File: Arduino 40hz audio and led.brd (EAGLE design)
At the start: 122.7 x 100 mm, 29 parts, among them IC1 LM7805, IC2 IRL-Z44N, IC3 LM741

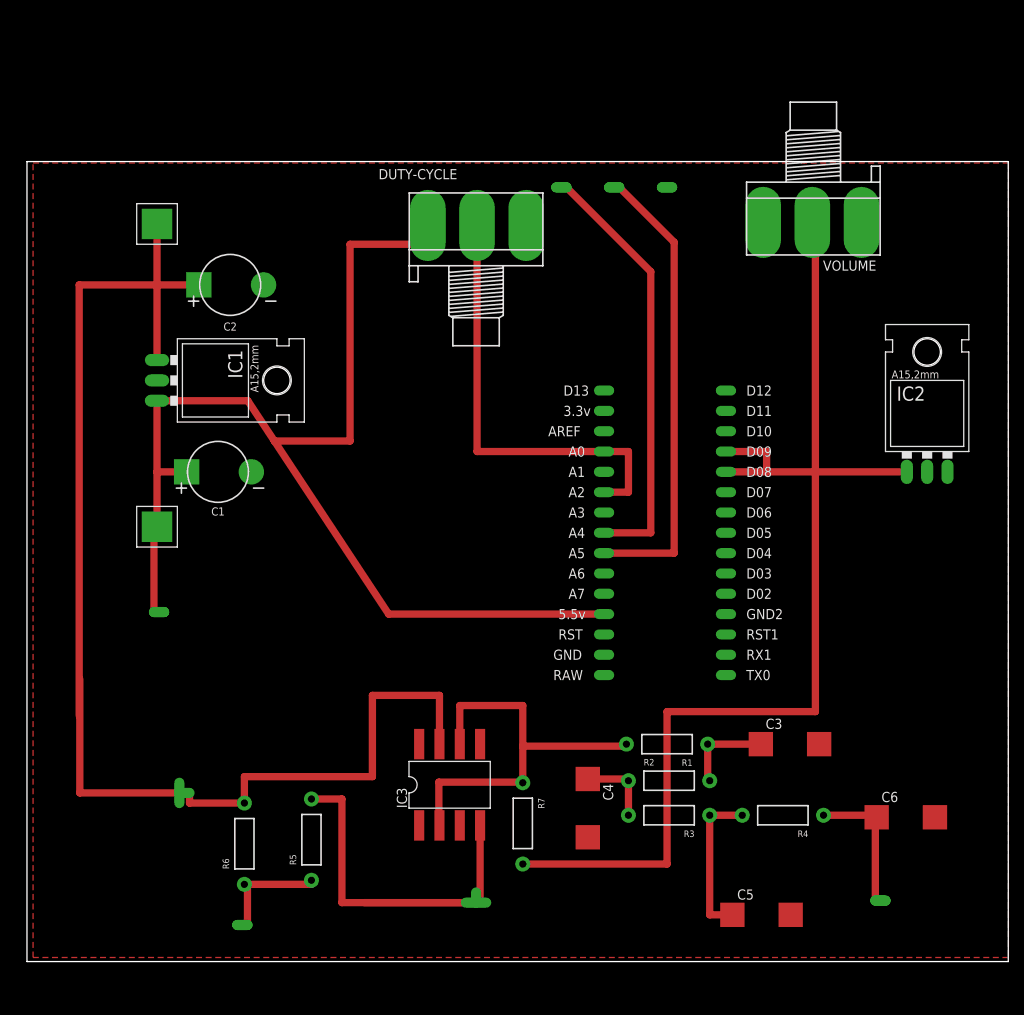
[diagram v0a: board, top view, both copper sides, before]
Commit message: Updated schematic and board
Updated schematic and board. Made the board more compact.

Still need to fix a few issues with the board
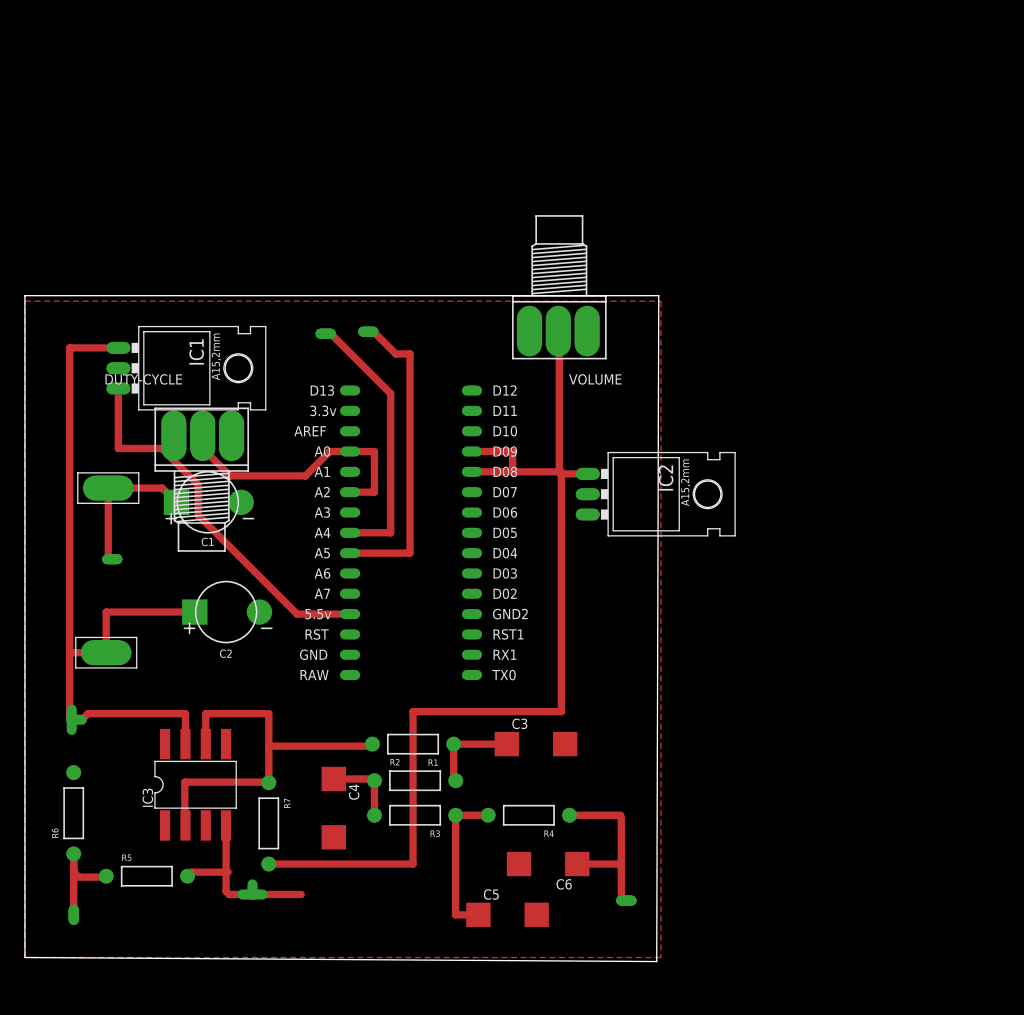
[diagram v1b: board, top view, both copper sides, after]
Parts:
- removed LCD-GND: LCD-GND, jim_muppet_parts:PAD-2PIN-RECTANGLE-50MIL
- moved P+1 54.0 mm to (9.91, 38.4), turned to 180 degrees
- moved C6 46.3 mm to (64.5, 11.9), turned to 180 degrees
- moved DUTY-CYCLE 42.8 mm to (21.8, 64.8)
- moved C2 40.9 mm to (24.9, 43.4)
- moved IC2 39.2 mm to (73.9, 58.2), turned to 270 degrees
- moved U$6 35.6 mm to (42.7, 78.5)
- moved VOLUME 34.8 mm to (66.5, 79.2)
- moved U$4 34.7 mm to (37.3, 78.2)
- moved R1 31.8 mm to (48.3, 26.9)
- moved U$1 31.8 mm to (50.5, 44.5)
- moved C3 31.8 mm to (64.3, 26.9)
- moved C4 31.8 mm to (38.4, 18.3)
- moved C5 31.8 mm to (60.7, 5.59)
- moved IC3 31.8 mm to (21.1, 21.8)
- moved R4 31.8 mm to (62.7, 18.0)
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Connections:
- net GND: no longer LCD-GND.PAD$2
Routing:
- net +5V: track 144.6 -> 68.5 mm
- net N$11: track 80.0 -> 26.5 mm
- net N$10: track 33.8 -> 5.29 mm
- net N$2: track 147.9 -> 123.8 mm
- net +12V: track 85.8 -> 64.9 mm
- net N$1: track 53.1 -> 32.3 mm
- net N$14: track 53.4 -> 33.1 mm
- net N$15: track 56.6 -> 37.4 mm
- net GND: track 24.3 -> 19.1 mm
- net N$6: track 18.7 -> 22.3 mm
- net N$13: track 51.5 -> 49.5 mm
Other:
- board size 122.7 x 100 mm -> 79.2 x 83.2 mm

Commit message: Version 1 is done.. w00t
Version 1 is done.. w00t!!!

Now I need to make some little fixes as I've built the first one.
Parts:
- added JP1: (no value), jumper:JP1
- added JP2, JP3: (no value), jim_muppet_parts:JP1
- added P+3: +6V, jim_muppet_parts:POWER-IN-PAD
- added R8: (no value), jim_muppet_parts:AXIAL-0.4
- U$2: value PAD-2PIN-RECTANGLE -> -6v test point; device jim_muppet_parts:PAD-2PIN-RECTANGLE-50MIL -> jim_muppet_parts:PROBE_POINT_1
- U$3: value PAD-3PIN-RECTANGLE50MIL -> SINE out; device jim_muppet_parts:PAD-3PIN-RECTANGLE-50MIL -> jim_muppet_parts:PROBE_POINT_1
- U$5: value PAD-3PIN-RECTANGLE50MIL -> +/- 6v virt gnd; device jim_muppet_parts:PAD-3PIN-RECTANGLE-50MIL -> jim_muppet_parts:PROBE_POINT_1
- U$8: value PAD-2PIN-RECTANGLE -> +6v test point; device jim_muppet_parts:PAD-2PIN-RECTANGLE-50MIL -> jim_muppet_parts:PROBE_POINT_1
- moved U$2 46.4 mm to (28.7, 3.56)
- moved U$3 45.1 mm to (72.9, 2.54), turned to 0 degrees
- moved U$8 33.0 mm to (22.1, 34.3), turned to 0 degrees
- moved U$5 27.6 mm to (14.2, 3.81), turned to 0 degrees
- moved U$4 26.7 mm to (36.8, 104.9), turned to 90 degrees
- moved IC1 26.5 mm to (17.8, 100.3)
- moved U$6 26.2 mm to (43.4, 104.6), turned to 90 degrees
- moved VOLUME 25.4 mm to (61.7, 104.1)
- moved DUTY-CYCLE 23.1 mm to (22.4, 87.9)
- moved IC2 20.8 mm to (69.3, 78.5)
- moved U$1 20.2 mm to (52.6, 64.5)
- moved R5 17.4 mm to (10.2, 27.2), turned to 90 degrees
- moved R6 14.8 mm to (19.8, 13.5), turned to 180 degrees
- moved P+2 14.5 mm to (10.2, 73.4)
- moved U$7 14.0 mm to (11.2, 64.0)
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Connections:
- removed net N$11: IC3.7, U$5.PAD$3
- removed net N$12: IC3.4, U$3.PAD$3
- new net N$16: JP1.2, R5.P$1, U$5.P$1
- net +12V: now also IC3.7, JP2.1, R5.P$2, U$8.P$1; no longer U$5.PAD$1
- net +5V: now also IC2.GND, JP3.2, P+3.VCC; no longer U$1.5V
- net GND: now also IC3.4, R6.P$1, U$2.P$1; no longer U$3.PAD$1
- net N$10: now also IC3.2, R7.P$1, R8.P$2; no longer R5.P$2, U$3.PAD$2
- net N$13: now also R8.P$1; no longer IC3.2, R7.P$1
- net N$2: now also VOLUME.2
- net N$6: no longer U$2.PAD$1
- net N$7: now also JP1.1; no longer U$5.PAD$2
- net N$8: now also JP2.2, U$1.RAW; no longer IC2.GND, VOLUME.2
- net N$9: now also JP3.1, U$1.5V; no longer R5.P$1, R6.P$1, U$8.PAD$2
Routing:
- net +12V: track 64.9 -> 156.1 mm
- net N$10: track 5.29 -> 33.6 mm
- net N$11: track 26.5 -> 0.00 mm
- net N$2: track 123.8 -> 143.5 mm
- net +5V: track 68.5 -> 86.9 mm
- net N$13: track 49.5 -> 33.8 mm
- net N$16: track 0.00 -> 14.5 mm
- net N$8: track 0.00 -> 8.74 mm
- net N$6: track 22.3 -> 14.8 mm
- net N$5: track 19.3 -> 12.8 mm
- net N$9: track 14.1 -> 20.6 mm
- net N$4: track 9.61 -> 15.8 mm
- net GND: track 19.1 -> 13.2 mm
- net N$3: track 11.5 -> 17.1 mm
- net N$14: track 33.1 -> 37.5 mm
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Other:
- board size 79.2 x 83.2 mm -> 79.2 x 109.7 mm

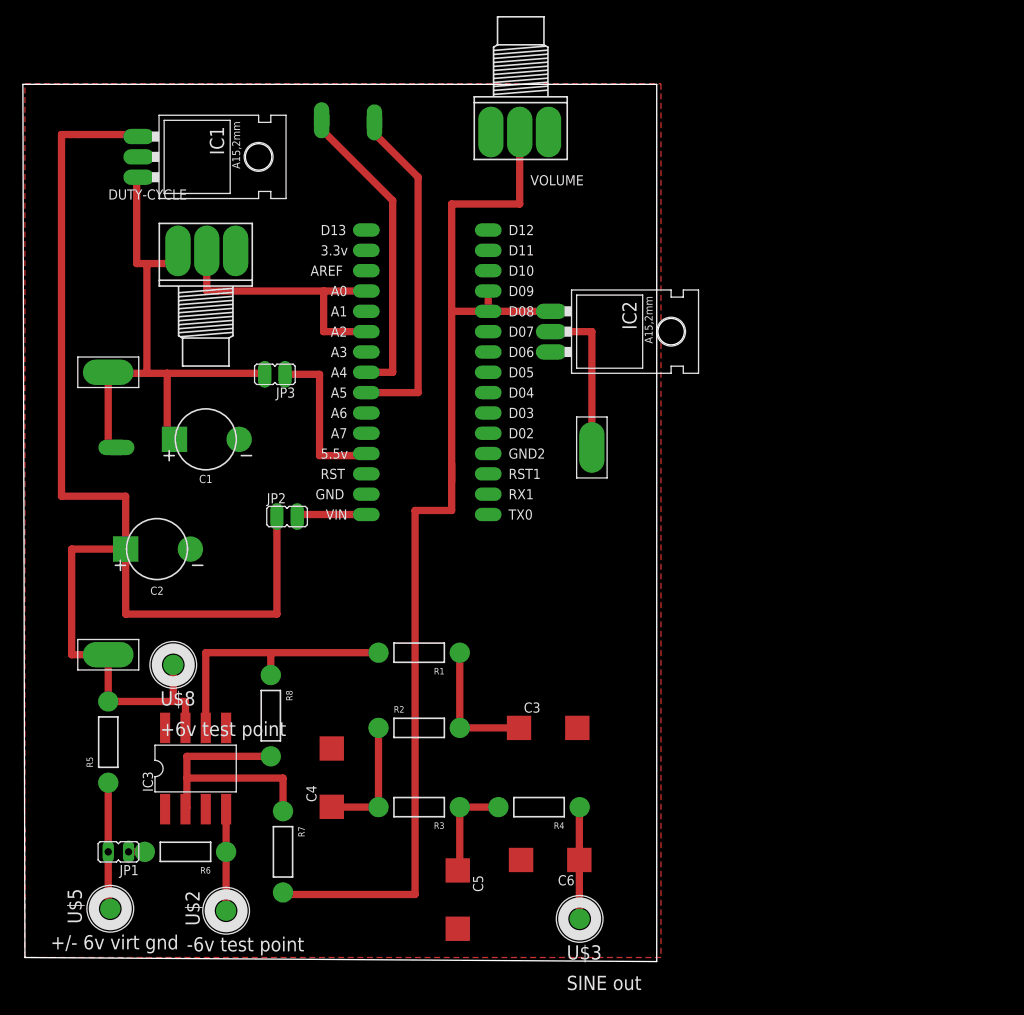
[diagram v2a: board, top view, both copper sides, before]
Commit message: Tagging this v1.0.1
Tagging this v1.0.1.
* Fixed the +/- 6v traces and placement.
* Changed a few pads to be larger
* Added a pad for the LED out signal from D5
* Removed Jumper JP1
* Added drill holes, those this will vary until you have exact PCB board
sizes.
* Added dimention markers for where the drill holes are to make it easier
in Fusion360 for when I make the case
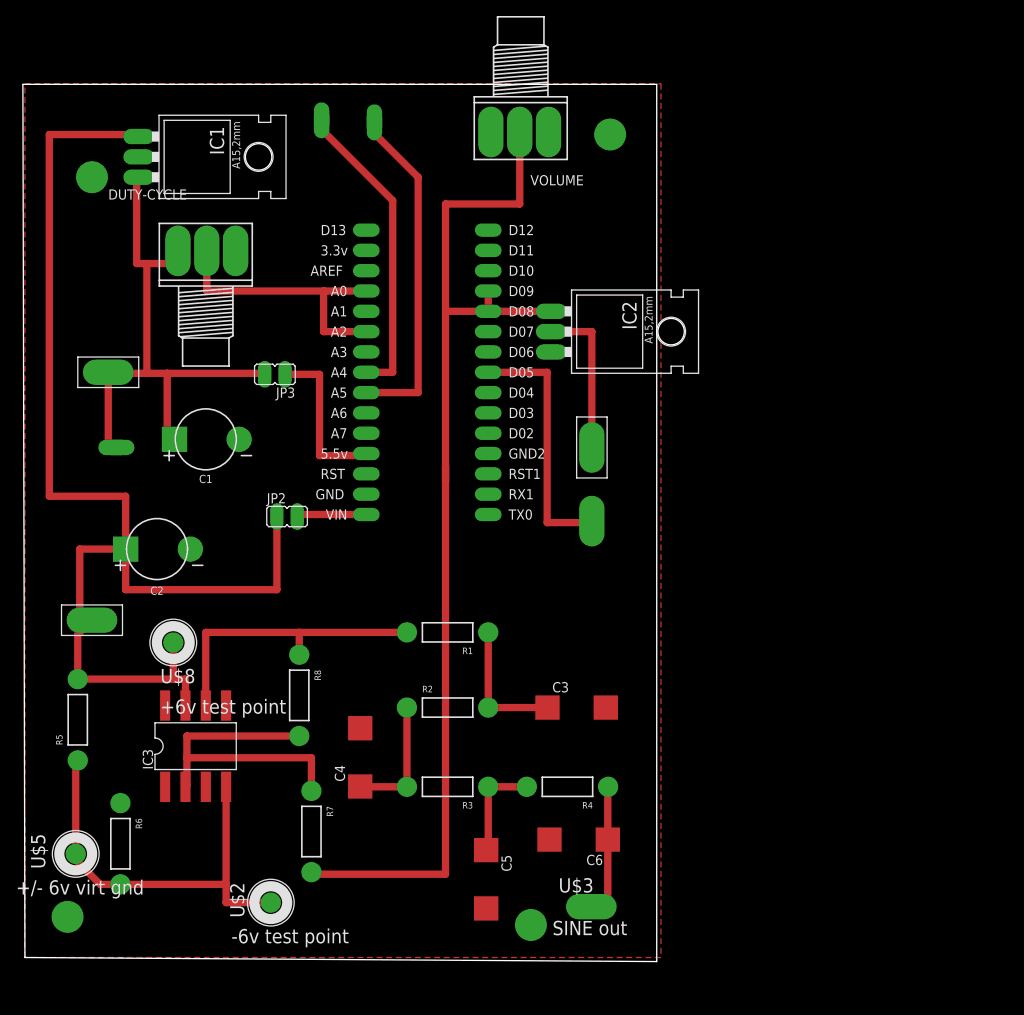
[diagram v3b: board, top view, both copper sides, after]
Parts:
- removed JP1: (no value), jumper:JP1
- added U$10, U$11, U$12, U$13: DRILL-HOLE-4MM, jim_muppet_parts:DRILL-HOLE-4MM
- added U$9: PAD-1PIN-RECTANGLE, jim_muppet_parts:PAD-1PIN-RECTANGLE-125MIL
- U$3: device jim_muppet_parts:PROBE_POINT_1 -> jim_muppet_parts:PAD-1PIN-RECTANGLE-125MIL
- moved R6 8.19 mm to (11.7, 14.5), turned to 270 degrees
- moved U$5 8.10 mm to (9.91, 10.7)
- moved U$2 5.68 mm to (34.3, 4.57)
- moved U$3 5.24 mm to (69.6, 6.60)
- moved P+1 4.77 mm to (8.13, 42.4)
- moved R5 4.72 mm to (6.35, 30.0)
- moved C5 4.37 mm to (57.4, 9.40)
- moved R1 4.37 mm to (52.6, 40.9)
- moved R2 4.37 mm to (52.6, 31.5)
- moved R3 4.37 mm to (52.6, 21.6)
- moved R7 4.37 mm to (35.6, 16.0)
- moved R8 4.37 mm to (34.0, 33.0)
- moved C4 4.37 mm to (41.7, 25.9)
- moved C6 4.37 mm to (68.3, 15.0)
- moved C3 4.37 mm to (69.3, 31.5)
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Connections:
- removed net N$16: JP1.2, R5.P$1, U$5.P$1
- removed net N$7: JP1.1, R6.P$2
- new net N$11: U$1.D5, U$9.PAD$1
- new net N$12: IC3.4, R5.P$1, R6.P$2, U$2.P$1, U$5.P$1
- net GND: no longer IC3.4, U$2.P$1
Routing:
- net N$12: track 0.00 -> 52.7 mm
- net N$11: track 0.00 -> 32.3 mm
- net N$16: track 14.5 -> 0.00 mm
- net GND: track 13.2 -> 0.00 mm
- net N$10: track 33.6 -> 40.4 mm
- net N$2: track 143.5 -> 137.9 mm
- net +12V: track 156.1 -> 150.7 mm
- net N$13: track 33.8 -> 37.1 mm
- net N$7: track 2.03 -> 0.00 mm

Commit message: This will be the final version of design
This will be the final version of design unless I come up with something
more amazing.  At this point I will just be making minor tweaks.

The next phase of this effort will be to go from sine to square via a
Schmitt trigger.
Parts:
- added U$14: PAD-1PIN-RECTANGLE175, jim_muppet_parts:PAD-RECTANGLE-175MIL
- R1, R2, R3, R4: value (none) -> 39k
- R5, R6: value (none) -> 1k
- R7: value (none) -> 600R
- R8: value (none) -> 4k
- U$3: device jim_muppet_parts:PAD-1PIN-RECTANGLE-125MIL -> jim_muppet_parts:PAD-RECTANGLE-200MIL
- U$4: value PAD-2PIN-RECTANGLE -> SCL; device jim_muppet_parts:PAD-2PIN-RECTANGLE-50MIL -> jim_muppet_parts:PAD-RECTANGLE-175MIL
- U$6: value PAD-2PIN-RECTANGLE -> PAD-1PIN-RECTANGLE175; device jim_muppet_parts:PAD-2PIN-RECTANGLE-50MIL -> jim_muppet_parts:PAD-RECTANGLE-175MIL
- U$9: value PAD-1PIN-RECTANGLE -> PAD-1PIN-RECTANGLE175; device jim_muppet_parts:PAD-1PIN-RECTANGLE-125MIL -> jim_muppet_parts:PAD-RECTANGLE-175MIL
- moved U$6 3.25 mm to (45.5, 102.1)
- moved U$4 3.07 mm to (38.1, 102.1)
- moved U$9 3.06 mm to (70.4, 50.8)
- moved U$3 2.90 mm to (72.4, 7.37), turned to 180 degrees
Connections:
- net N$14: no longer U$4.PAD$2
- net N$15: no longer U$6.PAD$2
- net N$2: now also U$14.PAD$1
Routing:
- net N$2: track 137.9 -> 159.0 mm
- net N$15: track 41.1 -> 38.3 mm
- net N$14: track 37.5 -> 35.1 mm
- net N$9: track 20.6 -> 19.3 mm
- net +5V: track 86.9 -> 85.7 mm
- net +12V: track 150.7 -> 150.0 mm
- net N$8: track 8.74 -> 9.43 mm
